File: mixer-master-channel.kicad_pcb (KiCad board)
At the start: 2 copper layers, 40.3 x 128.5 mm, 107 parts, among them J101 SEND_OUT, J102 HEADPHONE, Q801 Q_NPN_BCE, Q802 Q_PNP_BCE, Q803 Q_NPN_BCE, Q804 Q_PNP_BCE, U101 TL074, U1101 LM3916, U1102 LM3916, U301 TL074, U401 TL074, U501 TL074, U601 TL074, U701 TL074

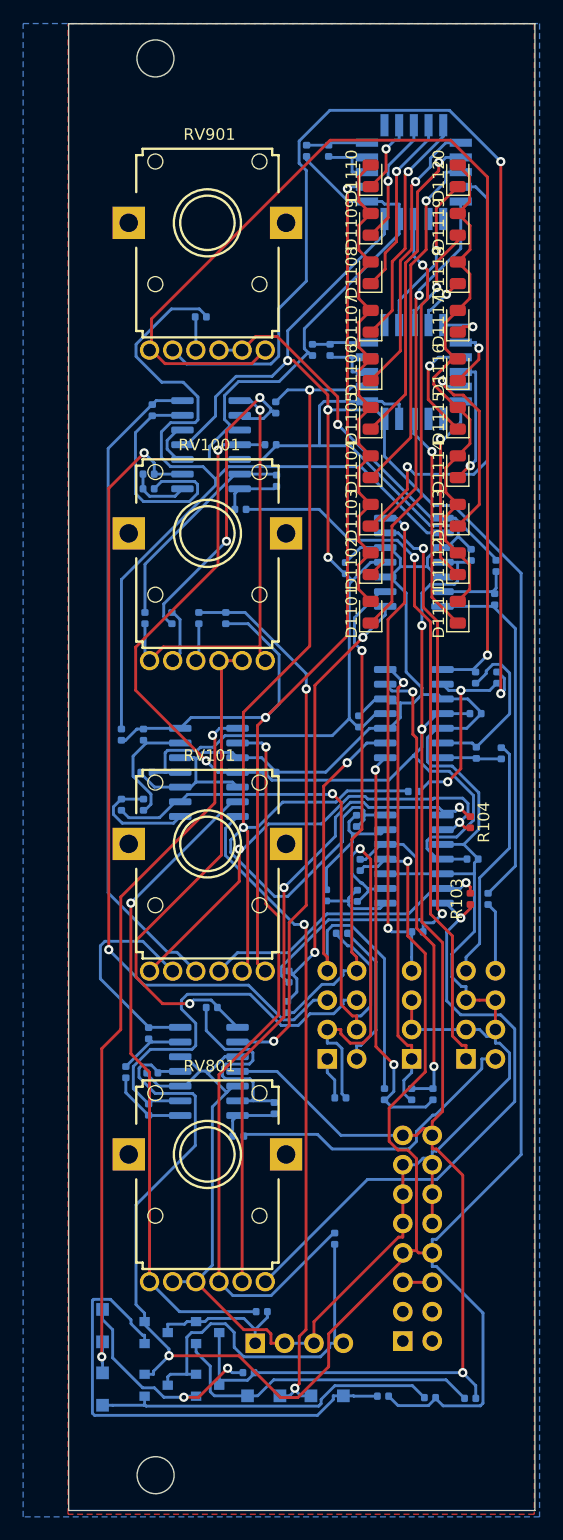
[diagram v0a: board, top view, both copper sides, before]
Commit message: Added buffer to CUEMIX
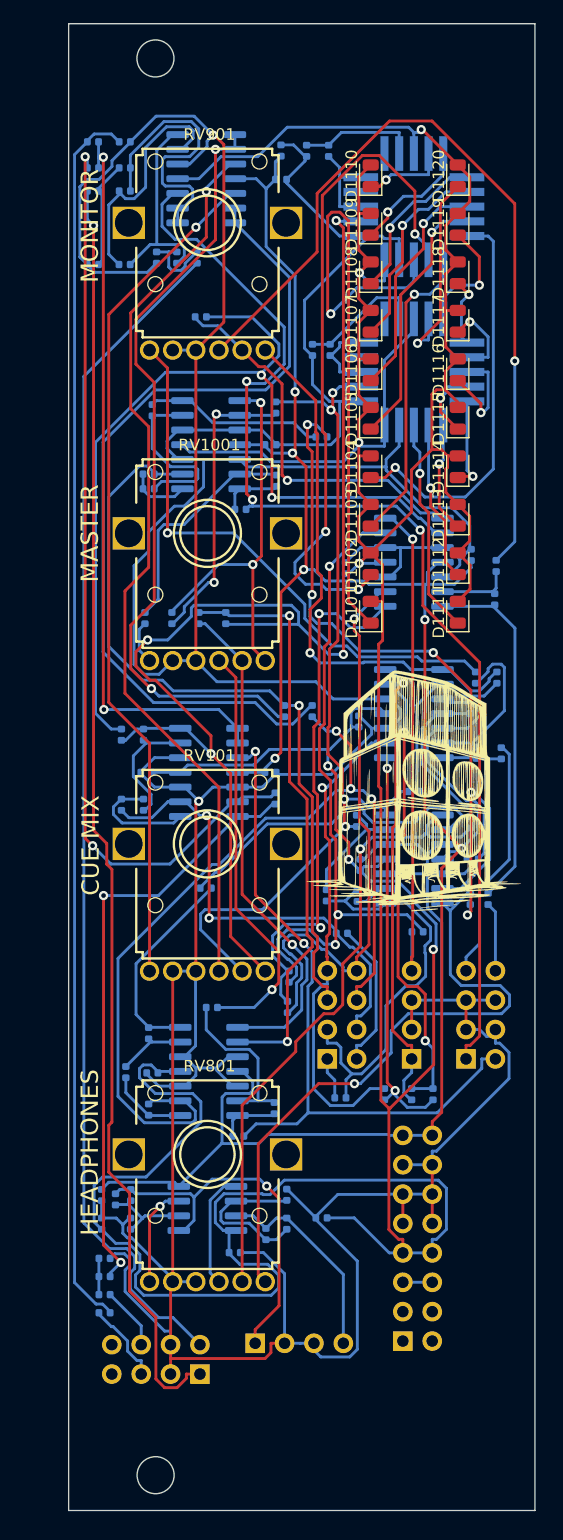
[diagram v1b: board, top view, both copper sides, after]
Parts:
- removed D801, D802, D803, D804: D, Diode_SMD:D_SOD-123F
- removed Q801, Q803: Q_NPN_BCE, Package_TO_SOT_SMD:SOT-23
- removed Q802, Q804: Q_PNP_BCE, Package_TO_SOT_SMD:SOT-23
- removed R805, R806: 1k, Resistor_SMD:R_0402_1005Metric
- removed R807, R808: 100k, Resistor_SMD:R_0402_1005Metric
- added C1201: 10u, Capacitor_SMD:C_0402_1005Metric, B.Cu at (117.0, 46.8)
- added C1202: 10u, Capacitor_SMD:C_0402_1005Metric, B.Cu at (121.5, 54.5)
- added C1203: 10u, Capacitor_SMD:C_0402_1005Metric, B.Cu at (114.2, 44.5)
- added C1204: 10u, Capacitor_SMD:C_0402_1005Metric, B.Cu at (115.2, 142.6)
- added C1205: 1u, Capacitor_SMD:C_0402_1005Metric, B.Cu at (134.0, 137.5)
- added C1206: 1u, Capacitor_SMD:C_0402_1005Metric, B.Cu at (130.5, 45.2)
- added C1207: 10u, Capacitor_SMD:C_0402_1005Metric, B.Cu at (126.5, 140.5)
- added C1208: 10u, Capacitor_SMD:C_0402_1005Metric, B.Cu at (130.5, 47.8)
- added C801: 47p, Capacitor_SMD:C_0402_1005Metric, B.Cu at (116.2, 135.9)
- added C802: 47p, Capacitor_SMD:C_0402_1005Metric, B.Cu at (129.2, 138.9)
- added C803: 0.1u, Capacitor_SMD:C_0402_1005Metric, B.Cu at (115.0, 138.0)
- added C804: 0.1u, Capacitor_SMD:C_0402_1005Metric, B.Cu at (115.0, 135.5)
- added G***: LOGO, components:gf, F.Cu at (142.0, 100.6)
- added J1201: BALANCED, Connector_PinHeader_2.54mm:PinHeader_2x04_P2.54mm_Vertical, B.Cu at (123.5, 151.0)
- added R105: 10k, Resistor_SMD:R_0402_1005Metric, B.Cu at (124.0, 109.0)
- added R106: 10k, Resistor_SMD:R_0402_1005Metric, B.Cu at (134.0, 70.0)
- added R107: 10k, Resistor_SMD:R_0402_1005Metric, B.Cu at (130.8, 93.7)
- added R108: 10k, Resistor_SMD:R_0402_1005Metric, B.Cu at (133.2, 93.7)
- added R1201: 10k, Resistor_SMD:R_0402_1005Metric, B.Cu at (117.0, 48.8)
- added R1202: 10k, Resistor_SMD:R_0402_1005Metric, B.Cu at (114.2, 46.8)
- added R1203: 10k, Resistor_SMD:R_0402_1005Metric, B.Cu at (117.0, 55.1)
- added R1204: 10k, Resistor_SMD:R_0402_1005Metric, B.Cu at (130.0, 101.2)
- added R1205: 10k, Resistor_SMD:R_0402_1005Metric, B.Cu at (114.2, 55.1)
- added R1206: 10k, Resistor_SMD:R_0402_1005Metric, B.Cu at (119.8, 54.5)
- added R1207: 10k, Resistor_SMD:R_0402_1005Metric, B.Cu at (117.0, 44.5)
- added R1208: 10k, Resistor_SMD:R_0402_1005Metric, B.Cu at (115.2, 141.0)
- added R1209: 1k, Resistor_SMD:R_0402_1005Metric, B.Cu at (114.2, 48.8)
- added R1210: 1k, Resistor_SMD:R_0402_1005Metric, B.Cu at (123.2, 54.5)
- added R1211: 1k, Resistor_SMD:R_0402_1005Metric, B.Cu at (115.2, 145.7)
- added R1212: 1k, Resistor_SMD:R_0402_1005Metric, B.Cu at (115.2, 144.1)
- added R801: 1k, Resistor_SMD:R_0402_1005Metric, B.Cu at (117.5, 138.0)
- added R802: 1k, Resistor_SMD:R_0402_1005Metric, B.Cu at (131.0, 135.5)
- added U1201: TL074, Package_SO:SOIC-14_3.9x8.7mm_P1.27mm, B.Cu at (124.0, 47.7)
- added U801: OPA1688, Package_SO:SOIC-8_3.9x4.9mm_P1.27mm, B.Cu at (124.1, 136.7)
- R1003, R1004, R903, R904: value 10k -> 50k
- R103, R104: moved to B.Cu
- R1102, R1104: value 7.5k -> 3.8k
- R803, R804: value 1k -> 6k
- U1101, U1102: footprint Package_LCC:PLCC-20 -> Package_LCC:PLCC-20-LongPads
- moved R803 27.9 mm to (117.5, 135.5), turned to 270 degrees
- moved R804 21.9 mm to (131.0, 138.0), turned to 270 degrees
- moved U1101 2.98 mm to (142.0, 50.1)
- turned R103 to 270 degrees
- turned R104 to 90 degrees
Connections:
- D1101 pad 2: Net-(D1101-Pad2) -> VDD
- D1102 pad 2: Net-(D1101-Pad2) -> VDD
- D1103 pad 2: Net-(D1101-Pad2) -> VDD
- D1104 pad 2: Net-(D1101-Pad2) -> VDD
- D1105 pad 2: Net-(D1101-Pad2) -> VDD
- D1106 pad 2: Net-(D1101-Pad2) -> VDD
- D1107 pad 2: Net-(D1101-Pad2) -> VDD
- D1108 pad 2: Net-(D1101-Pad2) -> VDD
- D1109 pad 2: Net-(D1101-Pad2) -> VDD
- D1110 pad 2: Net-(D1101-Pad2) -> VDD
- D1111 pad 2: Net-(D1111-Pad2) -> VDD
- D1112 pad 2: Net-(D1111-Pad2) -> VDD
- D1113 pad 2: Net-(D1111-Pad2) -> VDD
- D1114 pad 2: Net-(D1111-Pad2) -> VDD
- D1115 pad 2: Net-(D1111-Pad2) -> VDD
- D1116 pad 2: Net-(D1111-Pad2) -> VDD
- D1117 pad 2: Net-(D1111-Pad2) -> VDD
- D1118 pad 2: Net-(D1111-Pad2) -> VDD
- D1119 pad 2: Net-(D1111-Pad2) -> VDD
- D1120 pad 2: Net-(D1111-Pad2) -> VDD
- R803 pad 1: VDD -> /Sheet60360677/OUT_L
- R804 pad 1: Net-(D802-Pad1) -> /Sheet60360677/OUT_R
- R804 pad 2: VSS -> Net-(C802-Pad2)
- RV1001 pad 1: Net-(R1003-Pad1) -> GND
- RV1001 pad 3: Net-(R1005-Pad2) -> Net-(R1003-Pad1)
- RV1001 pad 4: Net-(R1004-Pad1) -> GND
- RV1001 pad 6: Net-(R1006-Pad2) -> Net-(R1004-Pad1)
- RV101 pad 1: /sheet6034D122/SUM -> GND
- RV101 pad 2: Net-(R104-Pad2) -> Net-(RV101-Pad2)
- RV101 pad 4: /sheet6034D121/SUM -> GND
- RV101 pad 5: Net-(R103-Pad2) -> Net-(RV101-Pad5)
- RV801 pad 2: Net-(R807-Pad1) -> Net-(RV801-Pad2)
- RV801 pad 5: Net-(R808-Pad1) -> Net-(RV801-Pad5)
- RV901 pad 1: Net-(R903-Pad1) -> GND
- RV901 pad 3: Net-(R905-Pad2) -> Net-(R903-Pad1)
- RV901 pad 4: Net-(R904-Pad1) -> GND
- RV901 pad 6: Net-(R906-Pad2) -> Net-(R904-Pad1)
- U1101 pad 10: Net-(D1110-Pad1) -> Net-(R1101-Pad2)
- U1101 pad 11: Net-(D1109-Pad1) -> VDD
- U1101 pad 12: Net-(D1108-Pad1) -> Net-(D1110-Pad1)
- U1101 pad 13: Net-(D1107-Pad1) -> Net-(D1109-Pad1)
- U1101 pad 14: Net-(D1106-Pad1) -> Net-(D1108-Pad1)
- U1101 pad 15: Net-(D1105-Pad1) -> Net-(D1107-Pad1)
- U1101 pad 16: Net-(D1104-Pad1) -> Net-(D1106-Pad1)
- U1101 pad 17: Net-(D1103-Pad1) -> Net-(D1105-Pad1)
- U1101 pad 18: Net-(D1102-Pad1) -> Net-(D1104-Pad1)
- U1101 pad 19: (no net) -> Net-(D1103-Pad1)
- U1101 pad 20: (no net) -> Net-(D1102-Pad1)
- U1101 pad 7: Net-(R1101-Pad1) -> (no net)
- U1101 pad 8: Net-(R1101-Pad2) -> Net-(R1101-Pad1)
- U1102 pad 10: Net-(D1120-Pad1) -> Net-(R1103-Pad2)
- U1102 pad 11: Net-(D1119-Pad1) -> VDD
- U1102 pad 12: Net-(D1118-Pad1) -> Net-(D1120-Pad1)
- U1102 pad 13: Net-(D1117-Pad1) -> Net-(D1119-Pad1)
- U1102 pad 14: Net-(D1116-Pad1) -> Net-(D1118-Pad1)
- U1102 pad 15: Net-(D1115-Pad1) -> Net-(D1117-Pad1)
- U1102 pad 16: Net-(D1114-Pad1) -> Net-(D1116-Pad1)
- U1102 pad 17: Net-(D1113-Pad1) -> Net-(D1115-Pad1)
- U1102 pad 18: Net-(D1112-Pad1) -> Net-(D1114-Pad1)
- U1102 pad 19: (no net) -> Net-(D1113-Pad1)
- U1102 pad 20: (no net) -> Net-(D1112-Pad1)
- U1102 pad 7: Net-(R1103-Pad1) -> (no net)
- U1102 pad 8: Net-(R1103-Pad2) -> Net-(R1103-Pad1)
- U301 pad 10: GND -> MASTER_R
- U301 pad 13: Net-(R807-Pad1) -> Net-(R1202-Pad1)
- U301 pad 8: Net-(D803-Pad1) -> Net-(C1203-Pad2)
- U301 pad 9: Net-(R808-Pad1) -> Net-(C1203-Pad2)
- U401 pad 8: Net-(R905-Pad2) -> Net-(R903-Pad1)
- U501 pad 8: Net-(R906-Pad2) -> Net-(R904-Pad1)
- U601 pad 8: Net-(R1005-Pad2) -> Net-(R1003-Pad1)
- U701 pad 8: Net-(R1006-Pad2) -> Net-(R1004-Pad1)
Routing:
- net GND: track 318.5 -> 521.8 mm, vias 0 -> 2
- net /Sheet60B047F7/LP: track 0.00 -> 110.2 mm, vias 0 -> 1
- net Net-(C1203-Pad1): track 0.00 -> 106.6 mm
- net /Sheet60B047F7/LN: track 0.00 -> 103.6 mm
- net VDD: track 314.5 -> 396.7 mm, vias 5 -> 7
- net Net-(R1202-Pad1): track 0.00 -> 79.8 mm, vias 0 -> 2
- net Net-(RV101-Pad5): track 0.00 -> 78.6 mm, vias 0 -> 1
- net Net-(R108-Pad2): track 0.00 -> 73.9 mm
- net Net-(RV101-Pad2): track 0.00 -> 73.5 mm, vias 0 -> 1
- net Net-(R107-Pad1): track 0.00 -> 67.2 mm, vias 0 -> 2
- net Net-(R808-Pad1): track 64.1 -> 0.00 mm, vias 1 -> 0
- net Net-(C1203-Pad2): track 0.00 -> 63.9 mm, vias 0 -> 2
- net Net-(D803-Pad1): track 63.0 -> 0.00 mm, vias 2 -> 0
- net Net-(R807-Pad1): track 56.5 -> 0.00 mm, vias 1 -> 0
- net Net-(R903-Pad1): track 98.5 -> 47.0 mm, vias 2 -> 1
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- removed copper zone on B.Cu, net GND
- removed copper zone on F.Cu, net GND
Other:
- board text added: "+"
- board text added: "-"
- board text added: "BALANCED"
- board text added: "CUE"
- board text added: "CUE MIX"
- board text added: "HEADPHONES"
- board text added: "L"
- board text added: "MASTER"
- board text added: "MONITOR"
- board text added: "OUTPUTS"
- board text added: "R"
- board text added: "RETURN"
- board text added: "SENDOUT"
- board text added: "SENDS"
- board text added: "VSS GND GND GND VDD 5V"
